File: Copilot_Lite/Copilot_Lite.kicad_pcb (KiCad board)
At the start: 4 copper layers, 65 x 56 mm, 80 parts, among them J1 POWER_MODES, J11 SERIAL_MODE, J12 SERIAL_VOLTAGE_SELECT, J2 JACK_POWER_IN, J3 USB_POWER_IN, J4 USB_PC, J6 5V_ENABLE, J7 SERIAL_AND_GPIO, J8 JACK_POWER_OUT, J9 USB_POWER_OUT, Q1 BSS138, Q2 BUK7M27-80EX, Q3 BUK7M27-80EX, Q4 BSS138, Q5 BSS138, Q6 BSS138, Q7 BSS138, Q8 BSS138, Q9 BSS138, U1 LM74502, U2 LM74502, U3 AP2204K-ADJ, U4 AP2204K-ADJ, U5 FT230XS, U6 SN74LV1T125, U7 SN74LV1T125, U8 SN74LV1T125, U9 SN74LV1T125

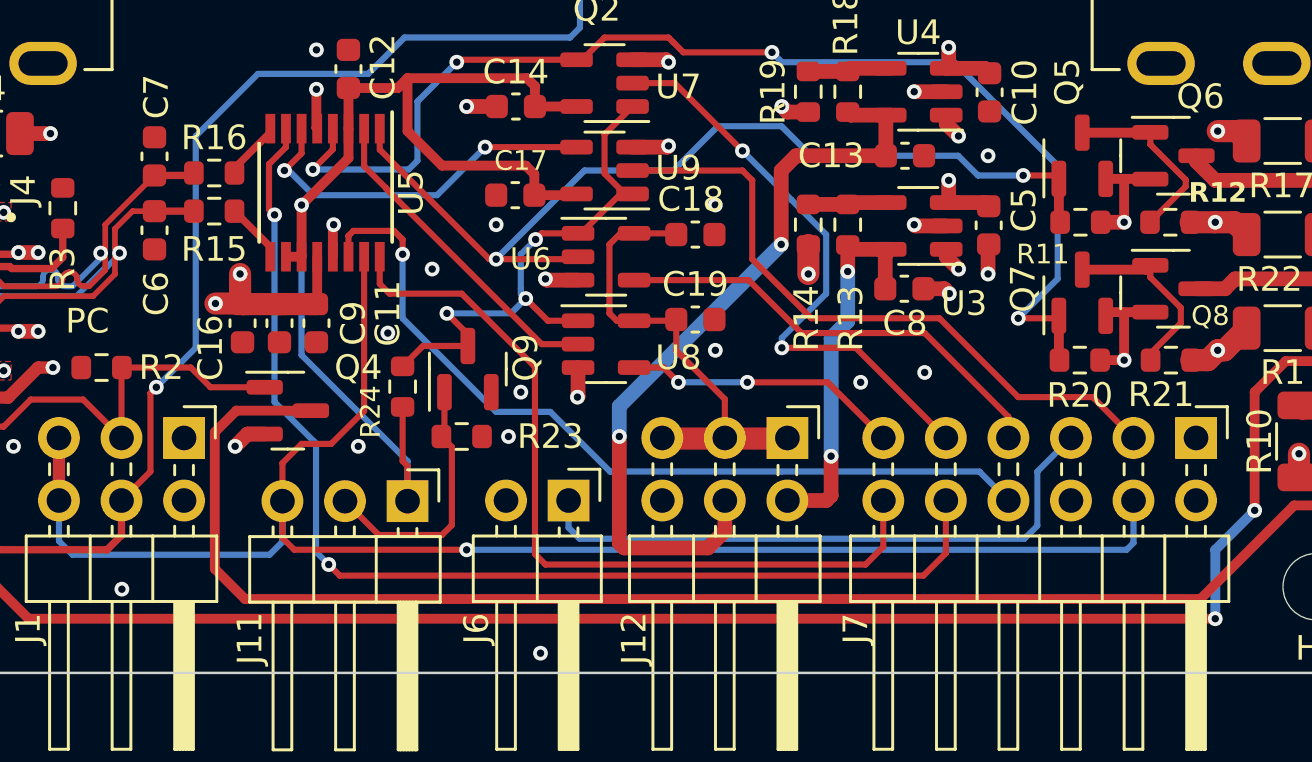
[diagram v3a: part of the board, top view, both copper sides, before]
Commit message: lite: Swapped UART and GPIO pin header rows in both schematic and PCB.
This allows to more easily use a mezzanine board.

It is now possible to solder a single row vertical pin header on the row
that is located inside the PCB and a right-angled single row pin header on
the row facing the PCB edge to still get access to the UART pins.
This way, the GPIOs can reach the mezzanine board and there is no need to
"forward" the UART signals to the mezzanine board.

Signed-off-by: Adrien Ricciardi <aricciardi@baylibre.com>
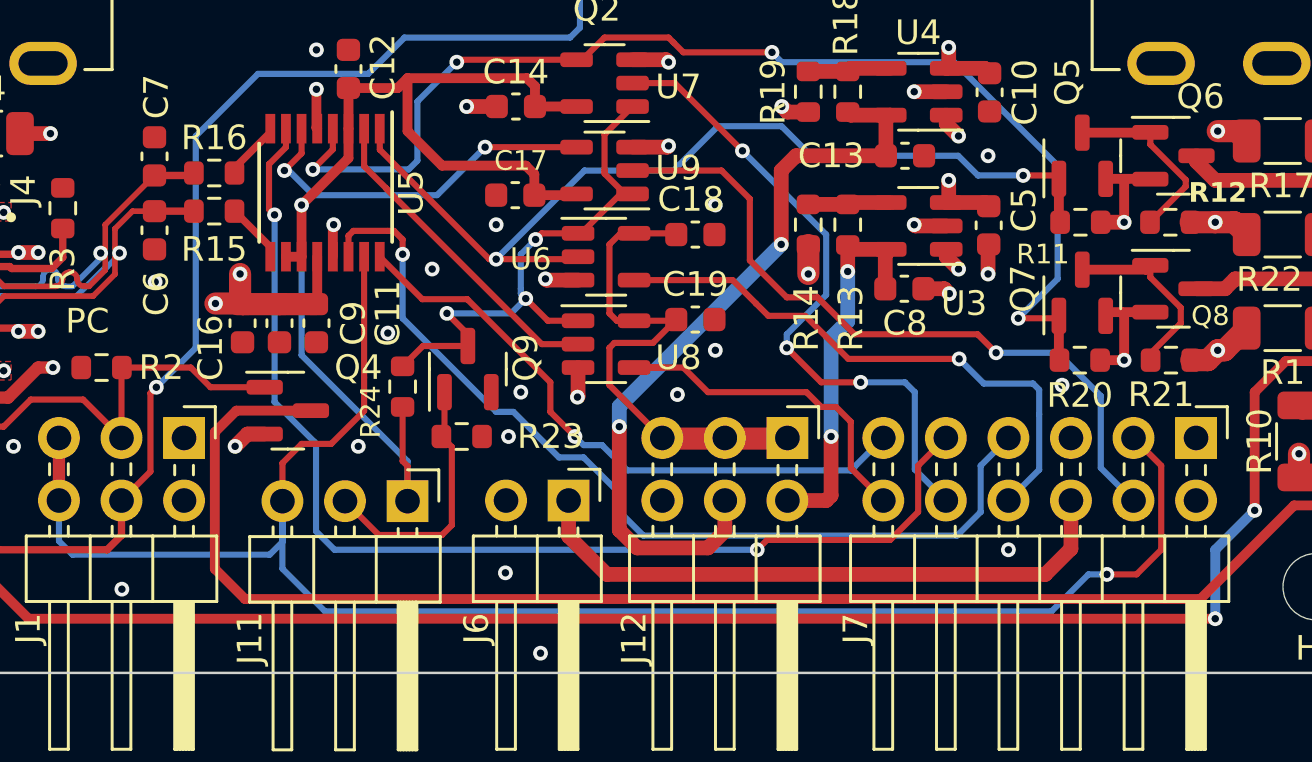
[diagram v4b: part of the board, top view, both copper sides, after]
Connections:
- J7 pad 10: /Controller/GPIO_2 -> /Controller/SERIAL_RX
- J7 pad 11: /Controller//SERIAL_RTS -> /Controller/GPIO_3
- J7 pad 12: /Controller/GPIO_3 -> /Controller//SERIAL_RTS
- J7 pad 3: /Controller//SERIAL_CTS -> /Controller/GPIO_0
- J7 pad 4: /Controller/GPIO_0 -> /Controller//SERIAL_CTS
- J7 pad 5: Net-(J6-Pin_1) -> +5V
- J7 pad 6: +5V -> Net-(J6-Pin_1)
- J7 pad 7: /Controller/SERIAL_TX -> /Controller/GPIO_1
- J7 pad 8: /Controller/GPIO_1 -> /Controller/SERIAL_TX
- J7 pad 9: /Controller/SERIAL_RX -> /Controller/GPIO_2
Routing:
- net /Controller/GPIO_3: track 32.9 -> 25.7 mm, vias 0 -> 1
- net /Controller/GPIO_0: track 65.5 -> 72.6 mm
- net /Controller/SERIAL_TX: track 18.4 -> 23.3 mm, vias 0 -> 1
- net /Controller/GPIO_1: track 34.1 -> 37.9 mm
- net /Controller//SERIAL_RTS: track 11.3 -> 14.7 mm, vias 2 -> 0
- net /Controller/SERIAL_RX: track 23.9 -> 26.5 mm, vias 2 -> 3
- net /Controller//SERIAL_CTS: track 26.7 -> 29.1 mm, vias 0 -> 1
- net /Controller/SERIAL_VOLTAGE: track 19.3 -> 21.4 mm
- net GND: vias 60 -> 63
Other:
- board text added: "+5V*"
- board text removed: "+5V (see J6)"

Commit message: lite: Improved reading of the bottom side documentation text on PCB silkscreen.
Signed-off-by: Adrien Ricciardi <aricciardi@baylibre.com>
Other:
- board text added: "UART enable Fit 1-2: always Fit 2-3: with channel"
- board text added: "UART voltage Fit 1-2: +1.8V Fit 3-4: +3.3V Fit 5-6: +5V"
- board text removed: "Fit 1-2: UART always enabled Fit 2-3: UART enabled with channel"
- board text removed: "Fit 1-2: UART voltage = +1.8V Fit 3-4: UART voltage = +3.3V Fit 5-6: UART voltage = +5V"
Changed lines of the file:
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@@
   (gr_rect (start 92.6 105) (end 97.2 107)
     (stroke (width 0.15) (type solid)) (fill solid) (layer "B.SilkS"))
-  (gr_line (start 104 102.6) (end 104 100.2)
+  (gr_line (start 103.735 102.586) (end 103.735 98.762)
     (stroke (width 0.4) (type default)) (layer "B.SilkS"))
   (gr_poly
@@
   (gr_arc (start 65 60) (mid 65.87868 57.87868) (end 68 57)
     (stroke (width 0.1) (type default)) (layer "Edge.Cuts"))
-  (gr_text "Fit to enable +5V on UART header" (at 94 104 270) (layer "B.SilkS" knockout)
+  (gr_text "Fit to enable +5V on\nUART header" (at 93.321 104 270) (layer "B.SilkS" knockout)
     (effects (font (size 1 1) (thickness 0.15)) (justify left bottom mirror))
   )
@@
     (effects (font (size 1 1) (thickness 0.15)) (justify left bottom mirror))
   )
-  (gr_text "Fit 1-2: UART always enabled\nFit 2-3: UART enabled with channel" (at 85.8 104 270) (layer "B.SilkS" knockout)
+  (gr_text "UART enable\nFit 1-2: always\nFit 2-3: with channel" (at 84.812 103.983 270) (layer "B.SilkS" knockout)
     (effects (font (size 1 1) (thickness 0.15)) (justify left bottom mirror))
   )
@@
     (effects (font (size 1 1) (thickness 0.15)) (justify right bottom mirror))
   )
-  (gr_text "Fit 1-2: UART voltage = +1.8V\nFit 3-4: UART voltage = +3.3V \nFit 5-6: UART voltage = +5V " (at 100.2 100 270) (layer "B.SilkS" knockout)
-    (effects (font (size 1 1) (thickness 0.15)) (justify left bottom mirror))
+  (gr_text "UART voltage\nFit 1-2: +1.8V\nFit 3-4: +3.3V \nFit 5-6: +5V " (at 99.544 98.776 270) (layer "B.SilkS" knockout)
+    (effects (font (size 1 1) (thickness 0.125)) (justify left bottom mirror))
   )
   (gr_text "1" (at 96.6 108.4) (layer "B.SilkS")

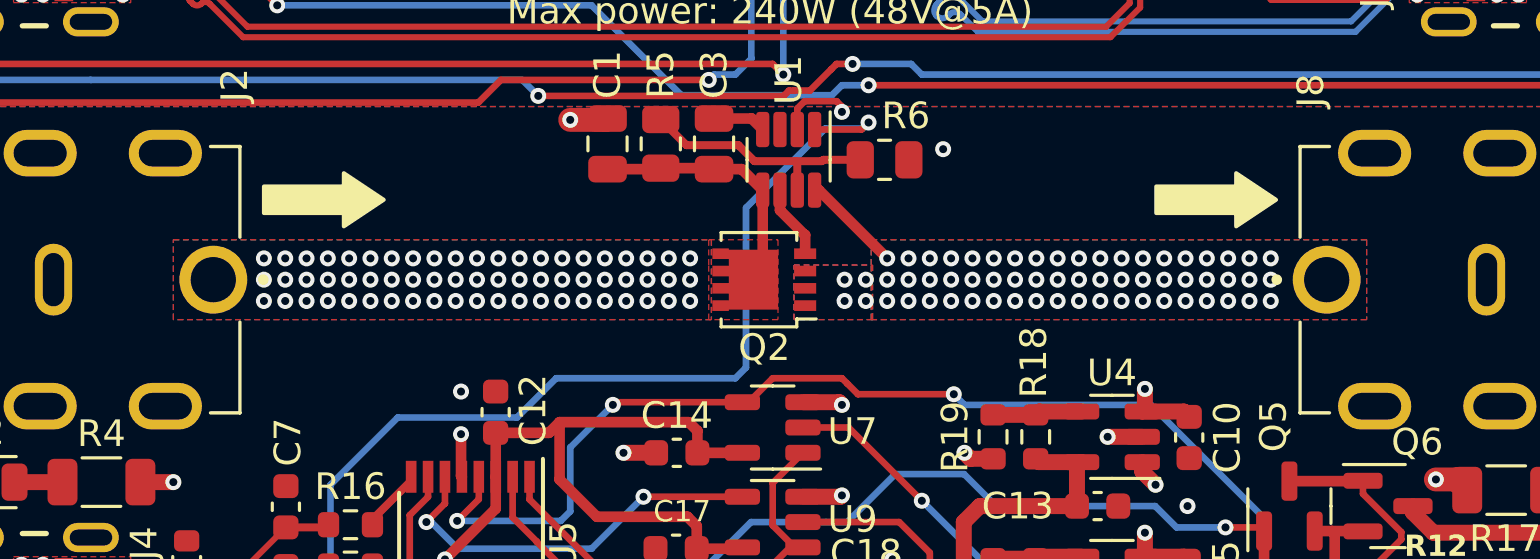
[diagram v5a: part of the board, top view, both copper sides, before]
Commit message: lite: Increased the trace width between the jack connectors to dissipate more heat.
Signed-off-by: Adrien Ricciardi <aricciardi@baylibre.com>
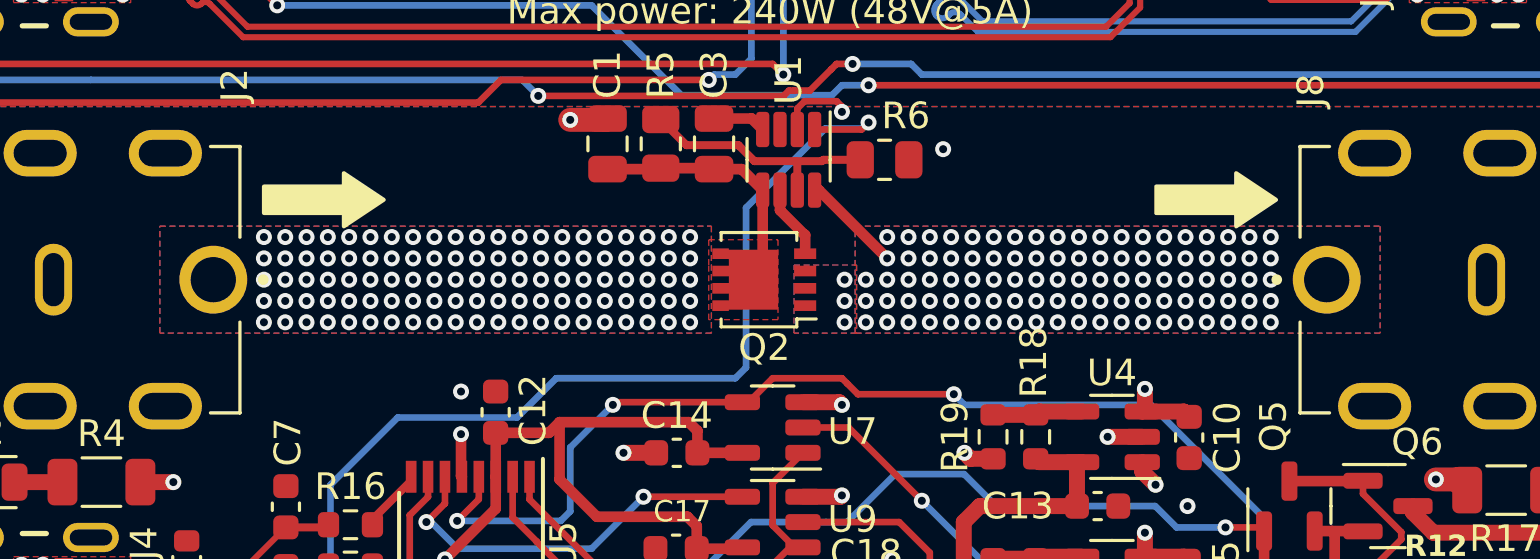
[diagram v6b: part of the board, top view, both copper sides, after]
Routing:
- net /Power Management/OUTPUT_JACK_V+: vias 61 -> 101
- net /Power Management/INPUT_JACK_V+: vias 63 -> 105
